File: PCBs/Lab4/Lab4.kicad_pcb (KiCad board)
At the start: 2 copper layers, 13 parts, among them IC1 M0C1103QDDFRQ1, J1 Conn_01x05_Pin, SW1 SW_SPST, SW2 SW_SPST

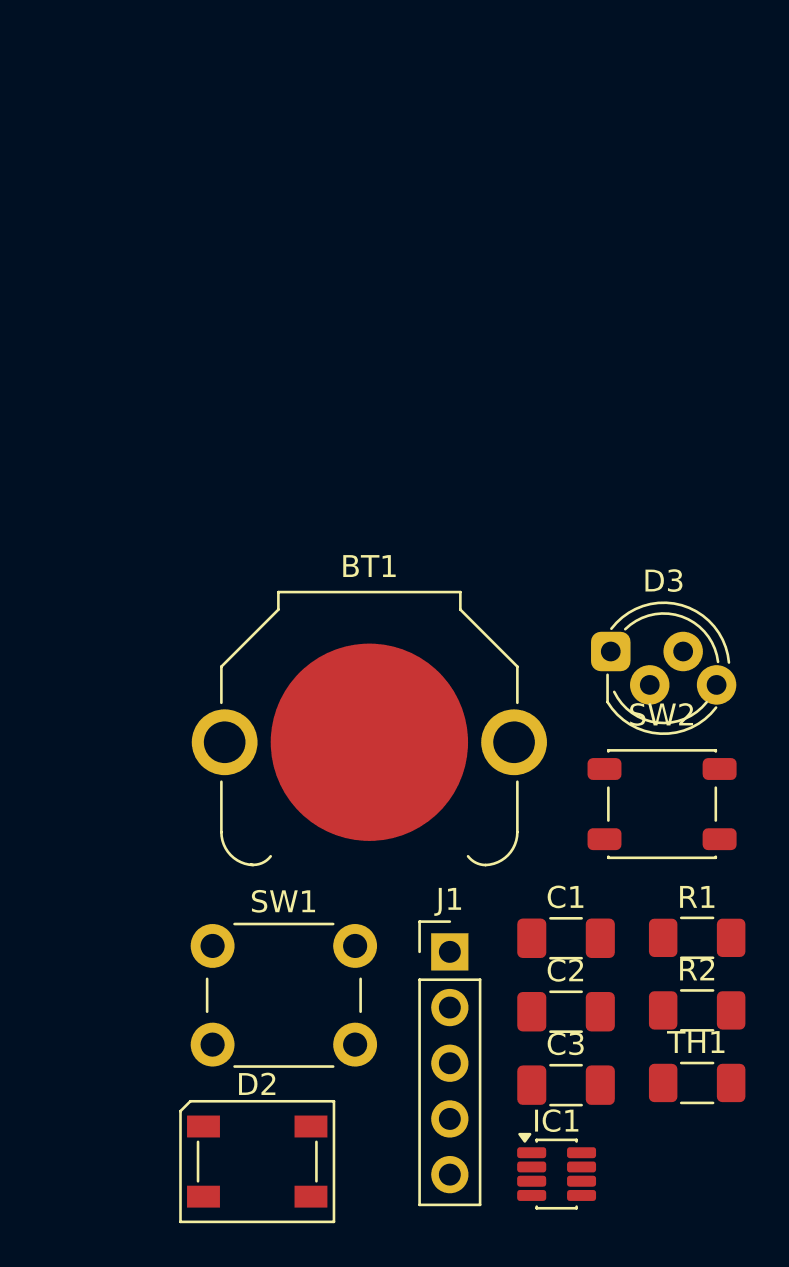
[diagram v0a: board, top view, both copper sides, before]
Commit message: Routed initial pcb submission
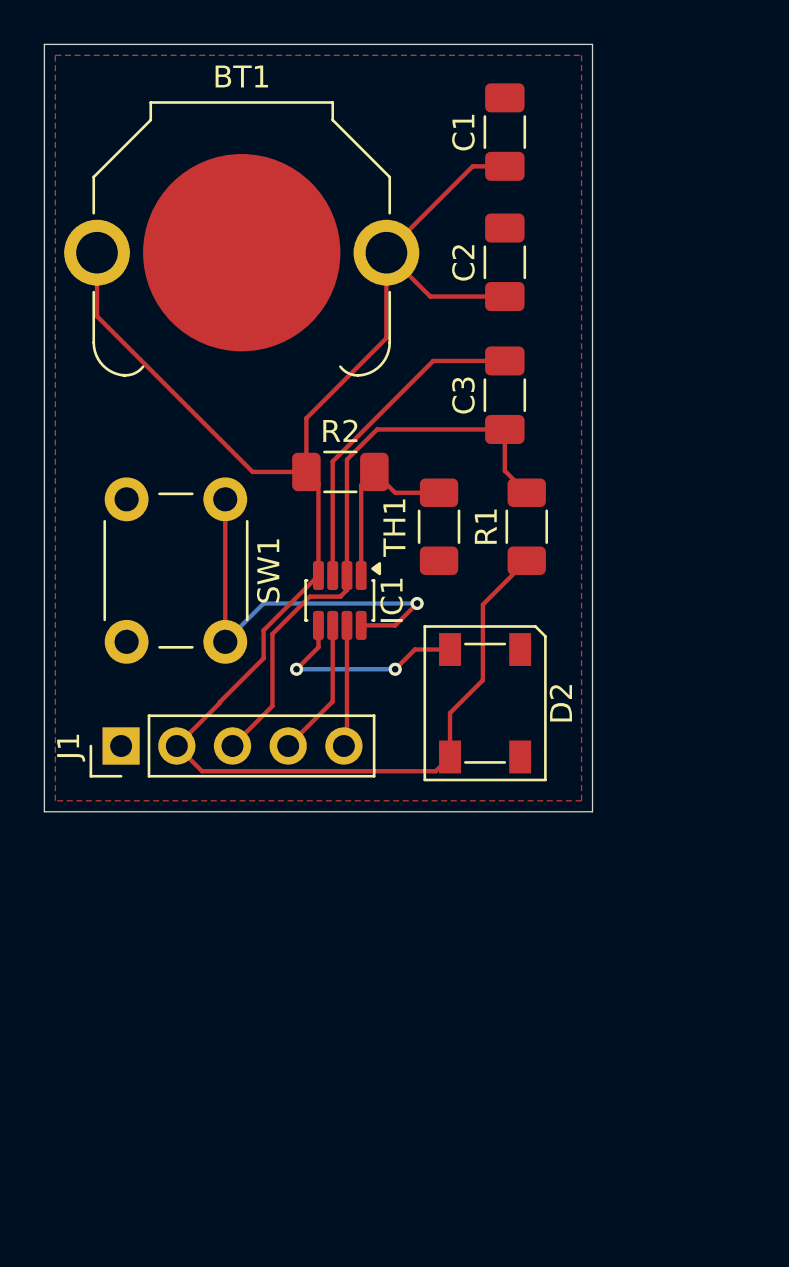
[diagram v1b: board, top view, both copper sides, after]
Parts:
- removed D3: NeoPixel_THT, LED_THT:LED_D5.0mm-4_RGB_Staggered_Pins
- removed SW2: SW_SPST, Button_Switch_SMD:SW_SPST_PTS647_Sx50
- moved C1 36.9 mm to (146.0, 65.0), turned to 90 degrees
- moved C2 34.3 mm to (146.0, 70.9), turned to 90 degrees
- moved C3 31.6 mm to (146.0, 77.0), turned to 90 degrees
- moved R2 29.5 mm to (138.5, 80.5)
- moved IC1 28.0 mm to (138.5, 86.4), turned to -90 degrees
- moved TH1 28.0 mm to (143.0, 83.0), turned to -90 degrees
- moved D2 23.3 mm to (145.1, 91.0), turned to -90 degrees
- moved BT1 23.1 mm to (134.0, 70.5)
- moved SW1 20.4 mm to (133.2, 81.8), turned to -90 degrees
- moved R1 20.3 mm to (147.0, 83.0), turned to 90 degrees
- moved J1 17.7 mm to (128.5, 93.0), turned to 90 degrees
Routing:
- net VDD: track 0.00 -> 79.2 mm
- net NRST: track 0.00 -> 28.1 mm
- net Button: track 0.00 -> 18.9 mm, vias 0 -> 1
- net GND: track 0.00 -> 15.0 mm
- net LED_DIN: track 0.00 -> 9.79 mm, vias 0 -> 2
- net THRM: track 0.00 -> 8.32 mm
- net SWDIO: track 0.00 -> 6.34 mm
- net SWCLK: track 0.00 -> 5.56 mm
- added copper zone on F.Cu, net GND
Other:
- board outline added: 25 x 35 mm

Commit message: Fixed routing for final submission
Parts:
- C3, R1: moved to B.Cu
- moved TH1 4.00 mm to (147.0, 83.0)
- moved R1 1.50 mm to (145.5, 83.0)
- turned BT1 to -90 degrees
- turned C2 to -90 degrees
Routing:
- net NRST: track 28.1 -> 37.9 mm, vias 0 -> 2
- net GND: track 15.0 -> 23.0 mm, vias 0 -> 1
- net THRM: track 8.32 -> 13.0 mm
- net LED_DIN: track 9.79 -> 8.08 mm
- net VDD: track 79.2 -> 77.8 mm, vias 0 -> 1
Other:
- board text added: "BS"
